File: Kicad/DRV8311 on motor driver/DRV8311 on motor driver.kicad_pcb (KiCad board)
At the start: 4 copper layers, 12.5 x 12.5 mm, 20 parts, among them J3 1mm pitch board edge, U2 DRV8311HRRWR

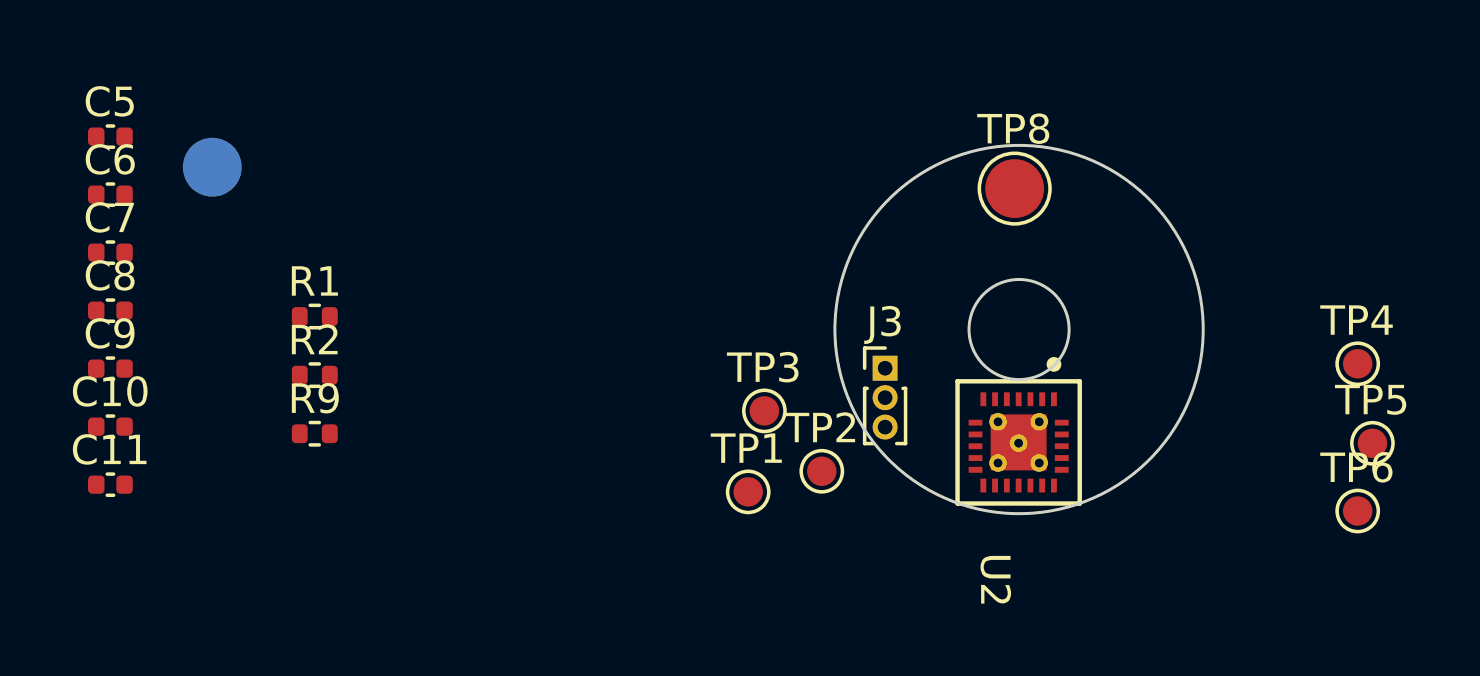
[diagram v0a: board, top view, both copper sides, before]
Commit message: Fixed kicad schematic errors, arranged pads
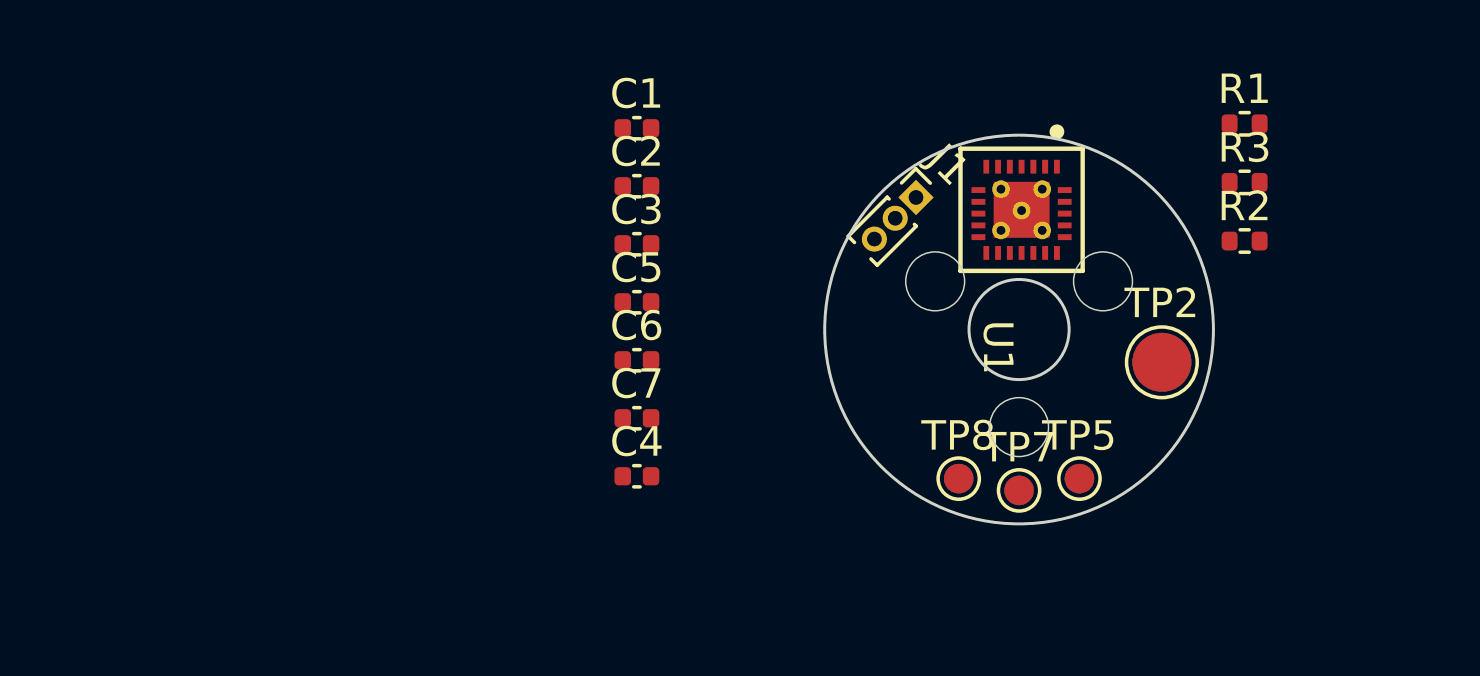
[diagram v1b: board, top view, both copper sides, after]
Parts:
- TP3: renamed from TP1; moved to B.Cu
- TP4: renamed from TP2; moved to B.Cu
- TP6: renamed from TP3; moved to B.Cu
- moved TP1 32.9 mm to (176.2, 101.5)
- moved R1 32.3 mm to (179.0, 93.5)
- moved R2 32.3 mm to (179.0, 97.4)
- moved R3 32.3 mm to (179.0, 95.4)
- moved C1 17.9 mm to (158.3, 93.6)
- moved C2 17.9 mm to (158.3, 95.6)
- moved C3 17.9 mm to (158.3, 97.5)
- moved C4 17.9 mm to (158.3, 105.4)
- moved C5 17.9 mm to (158.3, 99.5)
- moved C6 17.9 mm to (158.3, 101.5)
- moved C7 17.9 mm to (158.3, 103.5)
- moved TP8 13.6 mm to (169.2, 105.5)
- moved TP7 12.1 mm to (171.3, 105.9)
- moved TP6 10.9 mm to (173.3, 105.5), turned to 180 degrees
- moved TP5 10.2 mm to (173.3, 105.5)
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- renumbered C5 to C1, C6 to C2, C7 to C3, C11 to C4, C8 to C5, C9 to C6, C10 to C7, J3 to J1, R9 to R2, R2 to R3, TP7 to TP1, TP8 to TP2, TP4 to TP5, TP5 to TP7, TP6 to TP8, U2 to U1
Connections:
- C2 pad 1: unconnected-(#FLG02-Pad1) -> Net-(U1-CP)
- J1 pad 1: (no net) -> Net-(J1-Pin_1)
- J1 pad 2: (no net) -> Net-(J1-Pin_2)
- J1 pad 3: (no net) -> Net-(J1-Pin_3)
- R1 pad 1: (no net) -> Net-(U1-SLEEP_N)
- R2 pad 2: (no net) -> Net-(U1-SLEEP_N)
- R3 pad 2: (no net) -> Net-(U1-GAIN)
- TP3 pad 1: unconnected-(TP1-Pad1) -> Net-(U1-SOA)
- TP4 pad 1: unconnected-(TP2-Pad1) -> Net-(U1-SOB)
- TP5 pad 1: unconnected-(TP4-Pad1) -> Net-(U1-INHA)
- TP6 pad 1: unconnected-(TP3-Pad1) -> Net-(U1-SOC)
- TP7 pad 1: unconnected-(TP5-Pad1) -> Net-(U1-INHB)
- TP8 pad 1: unconnected-(TP6-Pad1) -> Net-(U1-INHC)
- U1 pad 1: (no net) -> unconnected-(U1-FAULT_N-Pad1)
- U1 pad 10: (no net) -> Net-(J1-Pin_1)
- U1 pad 11: (no net) -> Net-(J1-Pin_2)
- U1 pad 12: (no net) -> Net-(J1-Pin_3)
- U1 pad 13: unconnected-(TP6-Pad1) -> Net-(U1-INHC)
- U1 pad 14: unconnected-(TP5-Pad1) -> Net-(U1-INHB)
- U1 pad 15: unconnected-(TP4-Pad1) -> Net-(U1-INHA)
- U1 pad 21: (no net) -> Net-(U1-GAIN)
- U1 pad 22: (no net) -> unconnected-(U1-SLEW-Pad22)
- U1 pad 24: (no net) -> Net-(U1-SLEEP_N)
- U1 pad 3: unconnected-(TP3-Pad1) -> Net-(U1-SOC)
- U1 pad 4: unconnected-(TP2-Pad1) -> Net-(U1-SOB)
- U1 pad 5: unconnected-(TP1-Pad1) -> Net-(U1-SOA)
- U1 pad 6: unconnected-(#FLG02-Pad1) -> Net-(U1-CP)
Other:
- board size 12.5 x 12.5 mm -> 13.2 x 13.2 mm

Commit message: Finished component layout
The current board diameter is 12mm, though I may be able to shrink it down to 10mm. Its already REALLY small, with those 0402 components. It would be nice if the board didn't exceed the outer diameter of the motor.
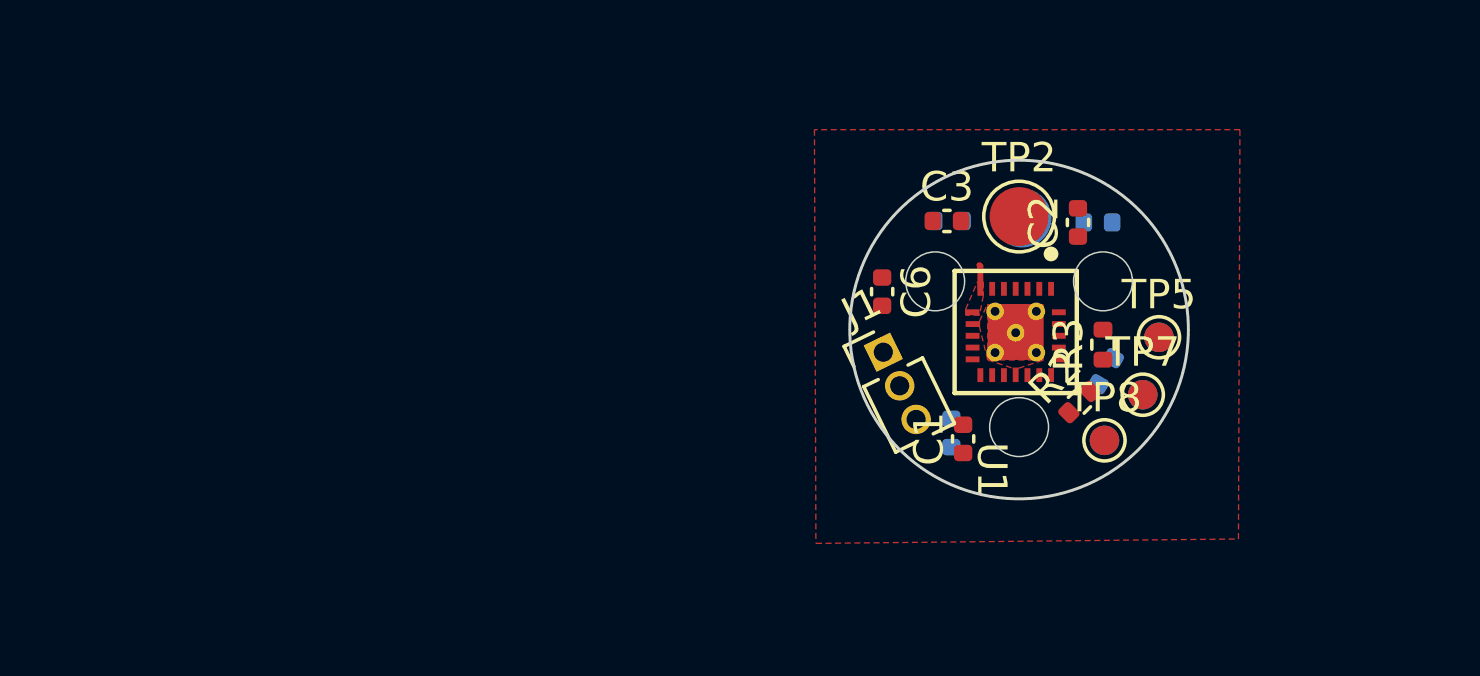
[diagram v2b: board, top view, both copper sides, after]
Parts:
- C4, C5, C7, R1: moved to B.Cu
- J1: footprint Connector_PinHeader_1.00mm:PinHeader_1x03_P1.00mm_Vertical -> Connector_PinHeader_1.27mm:PinHeader_1x03_P1.27mm_Vertical
- moved C5 15.9 mm to (174.0, 96.8)
- moved C1 15.3 mm to (169.4, 104.2), turned to 90 degrees
- moved C2 15.0 mm to (173.3, 96.8), turned to 90 degrees
- moved C4 13.7 mm to (168.9, 96.8), turned to 180 degrees
- moved C7 10.7 mm to (169.0, 104.0), turned to 90 degrees
- moved C3 10.6 mm to (168.8, 96.8)
- moved R1 9.63 mm to (174.2, 101.8), turned to 60 degrees
- moved C6 8.65 mm to (166.7, 99.2), turned to -90 degrees
- moved R2 7.84 mm to (173.3, 102.9), turned to 45 degrees
- moved R3 7.31 mm to (174.2, 101.0), turned to 90 degrees
- moved TP2 6.93 mm to (171.3, 96.6)
- moved TP1 6.82 mm to (171.4, 96.7)
- moved TP5 5.51 mm to (176.1, 100.7)
- moved TP6 5.51 mm to (176.1, 100.7)
- moved J1 5.37 mm to (166.7, 101.2), turned to 26 degrees
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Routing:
- net VDD: track 0.00 -> 0.82 mm
- added copper zone on F.Cu, net GND
- added copper zone on In1.Cu, net GND
- added copper zone on F.Cu, net VDD
- added copper zone on In2.Cu, net VDD
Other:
- board size 13.2 x 13.2 mm -> 11.5 x 11.5 mm

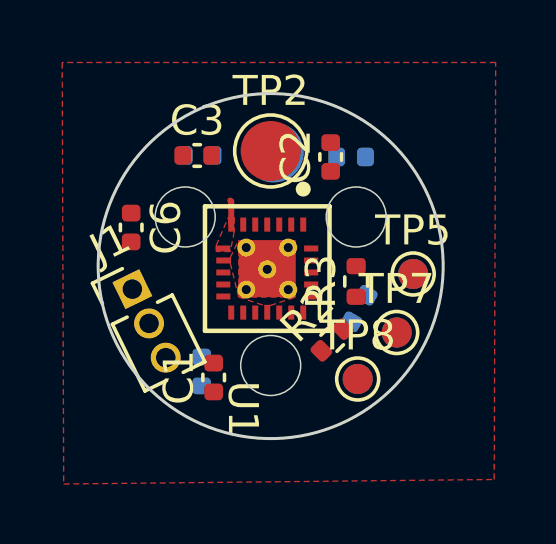
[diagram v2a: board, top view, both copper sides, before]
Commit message: Adding filled zones and mostly completed wiring
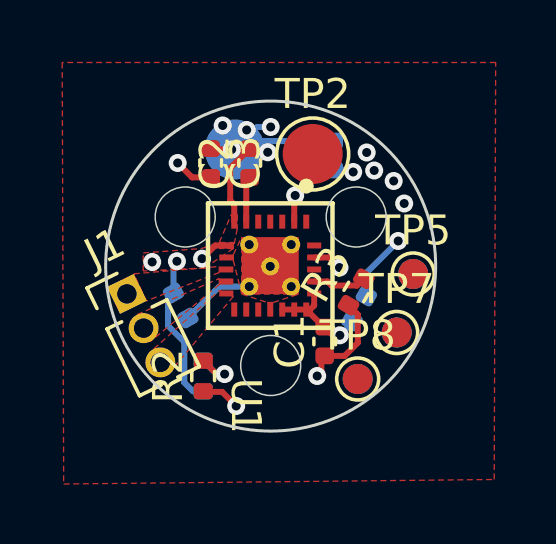
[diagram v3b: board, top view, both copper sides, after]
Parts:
- C6: moved to B.Cu
- moved R1 5.67 mm to (169.1, 104.1), turned to -90 degrees
- moved C7 5.65 mm to (174.2, 101.8), turned to -120 degrees
- moved R2 4.46 mm to (169.1, 104.1), turned to 90 degrees
- moved C1 3.89 mm to (173.1, 103.0)
- moved C4 3.55 mm to (172.4, 96.8), turned to -90 degrees
- moved C6 3.08 mm to (168.3, 101.8), turned to -60 degrees
- moved C2 2.71 mm to (170.6, 97.0)
- moved TP2 1.40 mm to (172.7, 96.7)
- moved TP1 1.30 mm to (170.1, 96.5)
- moved C5 0.58 mm to (173.4, 96.8), turned to -90 degrees
- moved C3 0.51 mm to (169.3, 97.0), turned to -90 degrees
- moved R3 0.35 mm to (174.2, 101.3), turned to 60 degrees
- moved J1 0.24 mm to (166.5, 101.4)
- moved U1 0.14 mm to (171.3, 100.4)
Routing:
- net VDD: track 0.82 -> 16.1 mm, vias 0 -> 8
- net GND: track 0.38 -> 12.6 mm, vias 0 -> 9
- net +3.3V: track 0.00 -> 11.5 mm, vias 0 -> 3
- net Net-(U1-GAIN): track 0.00 -> 1.81 mm
- net Net-(U1-SLEEP_N): track 0.00 -> 1.80 mm, vias 0 -> 1
- net Net-(U1-CP): track 0.00 -> 1.52 mm
- added copper zone on F.Cu, net Net-(J1-Pin_1)
- added copper zone on F.Cu, net Net-(J1-Pin_2)
- added copper zone on F.Cu, net Net-(J1-Pin_3)
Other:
- board size 11.5 x 11.5 mm -> 11 x 11 mm

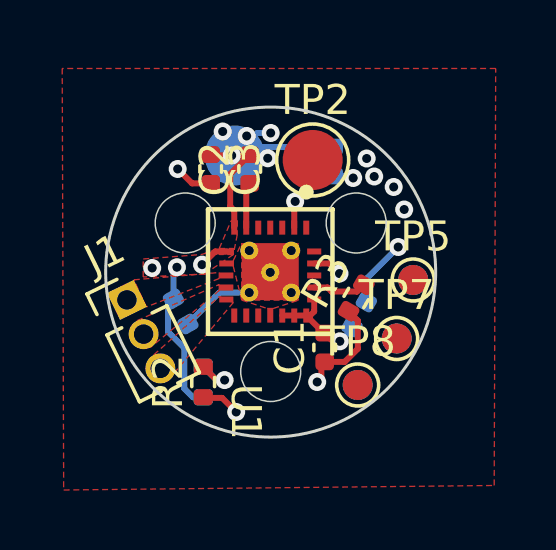
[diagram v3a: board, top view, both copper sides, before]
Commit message: Complex wire re-arranging
The most difficult to route wires are those last ones, the input and output wires. I have spent a long time figureing out an arrangement that would allow me to connect that. I wish I could add vias in the pads of the components, but that almost always spells disaster unless I pay more for capped vias. I am trying to get the smallest possible driver board while remain economical.
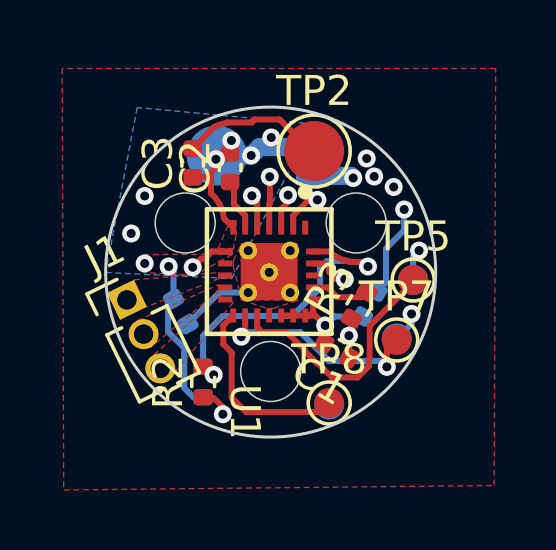
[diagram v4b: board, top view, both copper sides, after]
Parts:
- moved TP3 1.15 mm to (173.2, 104.8)
- moved TP8 1.12 mm to (173.2, 104.8)
- moved C2 0.65 mm to (169.9, 97.0)
- moved C3 0.63 mm to (168.7, 96.8), turned to 90 degrees
- moved TP1 0.60 mm to (169.5, 96.5)
- moved C7 0.49 mm to (174.6, 101.5)
- moved C1 0.41 mm to (173.5, 103.0), turned to 150 degrees
- moved TP2 0.30 mm to (172.8, 96.4)
- moved R3 0.27 mm to (174.2, 101.5)
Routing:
- net Net-(U1-SOB): track 0.00 -> 14.0 mm, vias 0 -> 2
- net Net-(U1-SOC): track 0.00 -> 13.8 mm, vias 0 -> 2
- net Net-(U1-SLEEP_N): track 1.80 -> 11.0 mm, vias 1 -> 2
- net Net-(U1-INHA): track 0.00 -> 8.46 mm
- net Net-(U1-INHB): track 0.00 -> 7.18 mm, vias 0 -> 2
- net Net-(U1-INHC): track 0.00 -> 6.56 mm
- net GND: track 12.6 -> 14.4 mm
- net Net-(U1-SOA): track 0.00 -> 1.14 mm, vias 0 -> 1
- net VDD: track 16.1 -> 16.7 mm, vias 8 -> 7
- added copper zone on B.Cu, net VDD

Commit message: Finished routing, distribute pwr planes, silkscreen and DRC check
The power planes were not making good connection previously, so I have fixed that.
Silkscreen is done, the last traces have been routed, and there isn't much I can do
As far as I'm concerned, this board is done!
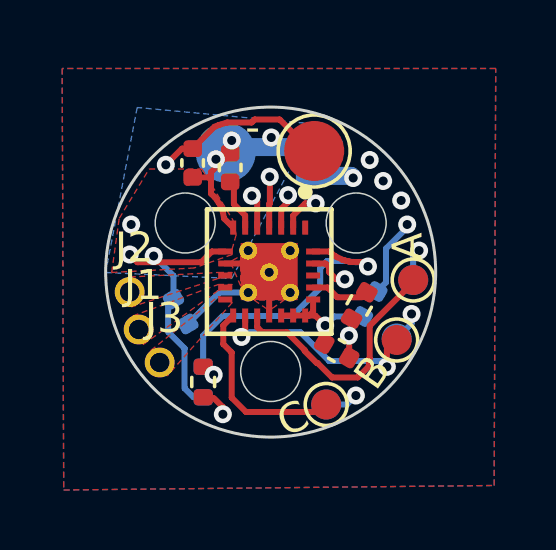
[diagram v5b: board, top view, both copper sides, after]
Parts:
- added J2: A, custom_testpoints:PinHeader_1x01_P1.27mm_Round, F.Cu at (166.6, 101.1)
- added J3: C, custom_testpoints:PinHeader_1x01_P1.27mm_Round, F.Cu at (167.6, 103.5)
- J1: value 1mm pitch board edge -> B; footprint Connector_PinHeader_1.27mm:PinHeader_1x03_P1.27mm_Vertical -> custom_testpoints:PinHeader_1x01_P1.27mm_Round
- moved J1 1.06 mm to (166.9, 102.3), turned to 0 degrees
- moved TP1 0.32 mm to (169.8, 96.5)
- moved TP8 0.11 mm to (173.2, 104.8)
- moved TP3 0.10 mm to (173.2, 104.8)
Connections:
- U1 pad 10: Net-(J1-Pin_1) -> Net-(J2-Pin_1)
- U1 pad 11: Net-(J1-Pin_2) -> Net-(J1-Pin_1)
- U1 pad 12: Net-(J1-Pin_3) -> Net-(J3-Pin_1)
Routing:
- net Net-(U1-SOA): track 1.14 -> 13.9 mm, vias 1 -> 2
- net GND: track 14.4 -> 17.6 mm, vias 9 -> 8
- net VDD: track 16.7 -> 19.0 mm, vias 7 -> 6
- added copper zone on B.Cu, net GND
- added copper zone on F.Cu, net Net-(J2-Pin_1)
- added copper zone on F.Cu, net Net-(J3-Pin_1)
- removed copper zone on F.Cu, net Net-(J1-Pin_2)
- removed copper zone on F.Cu, net Net-(J1-Pin_3)
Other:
- board text added: "+"
- board text added: "C"

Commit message: Fixed small issue on Driver board resistor values swapped
I switched it from 100k over 300k, to 300k over 100k. If the input is 8.4 volts, the output should be 2.1 volts. Small mistake.
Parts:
- R1: value 100k -> 300k
- R2: value 300k -> 100k
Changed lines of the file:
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@@
 		(tags "capacitor")
 		(property "Reference" "C1"
-			(at -1.557532 -0.197724 240)
+			(at -1.557532 -0.197724 -120)
 			(layer "F.SilkS")
 			(hide yes)
@@
 		(tags "DRV8311PRRWR ")
 		(property "Reference" "U1"
-			(at 0.430001 2.7 270)
+			(at 0.430001 2.7 -90)
 			(unlocked yes)
 			(layer "F.SilkS")
@@
 			)
 		)
-		(property "Value" "300k"
+		(property "Value" "100k"
 			(at 0 1.17 90)
 			(layer "F.Fab")
@@
 			)
 		)
-		(property "Value" "100k"
+		(property "Value" "300k"
 			(at 0 -1.17 90)
 			(layer "B.Fab")
